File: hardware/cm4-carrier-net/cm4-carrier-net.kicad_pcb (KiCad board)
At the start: 4 copper layers, 90 x 40 mm, 42 parts, among them J1 USB_C_Receptacle_USB2.0, J2 Micro_SD_Card, J3 Abracon_ARJM11-502, Q1 DMP2066LSN, SW1 BOOT, SW2 GLOBAL_EN, U5 Compute_Module_4_Functional, U6 TPD2EUSB30

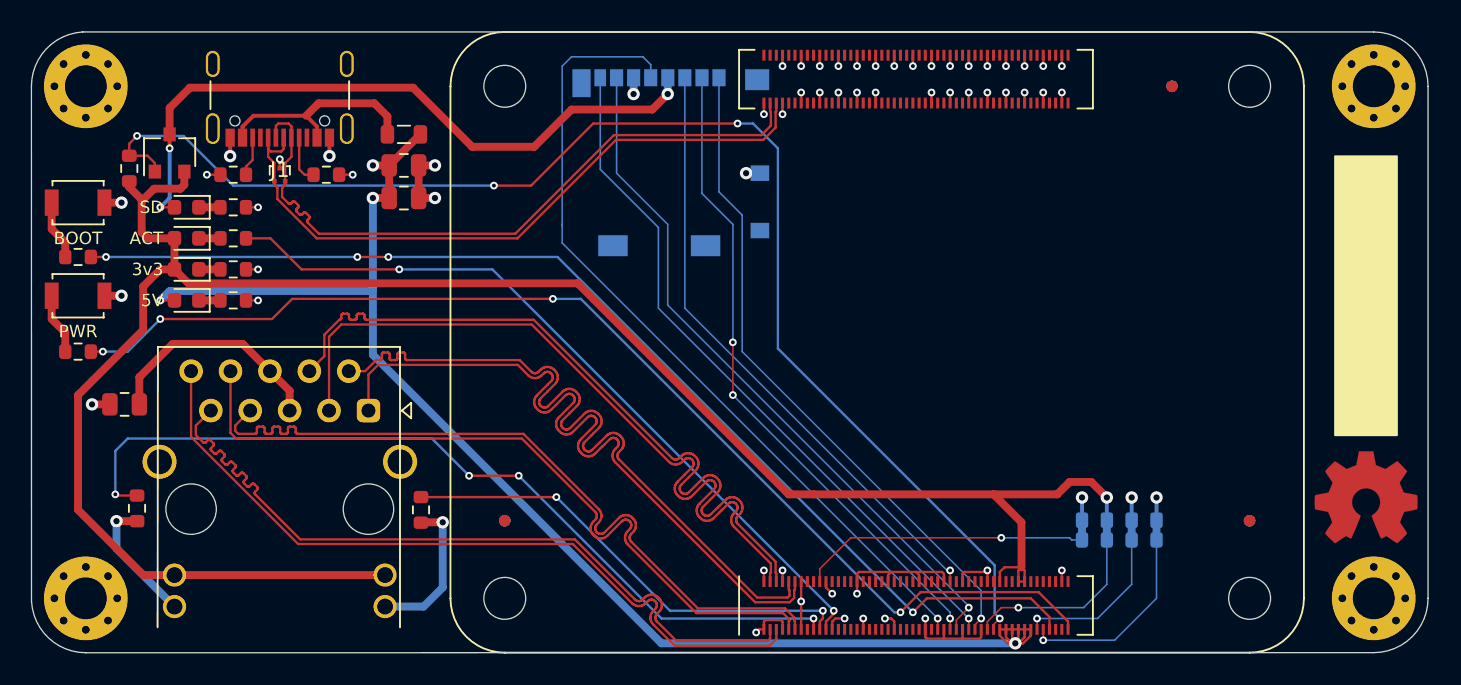
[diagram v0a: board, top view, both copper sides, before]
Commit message: Added USB OTG ID selection switch. Likely finalized v1.0a.
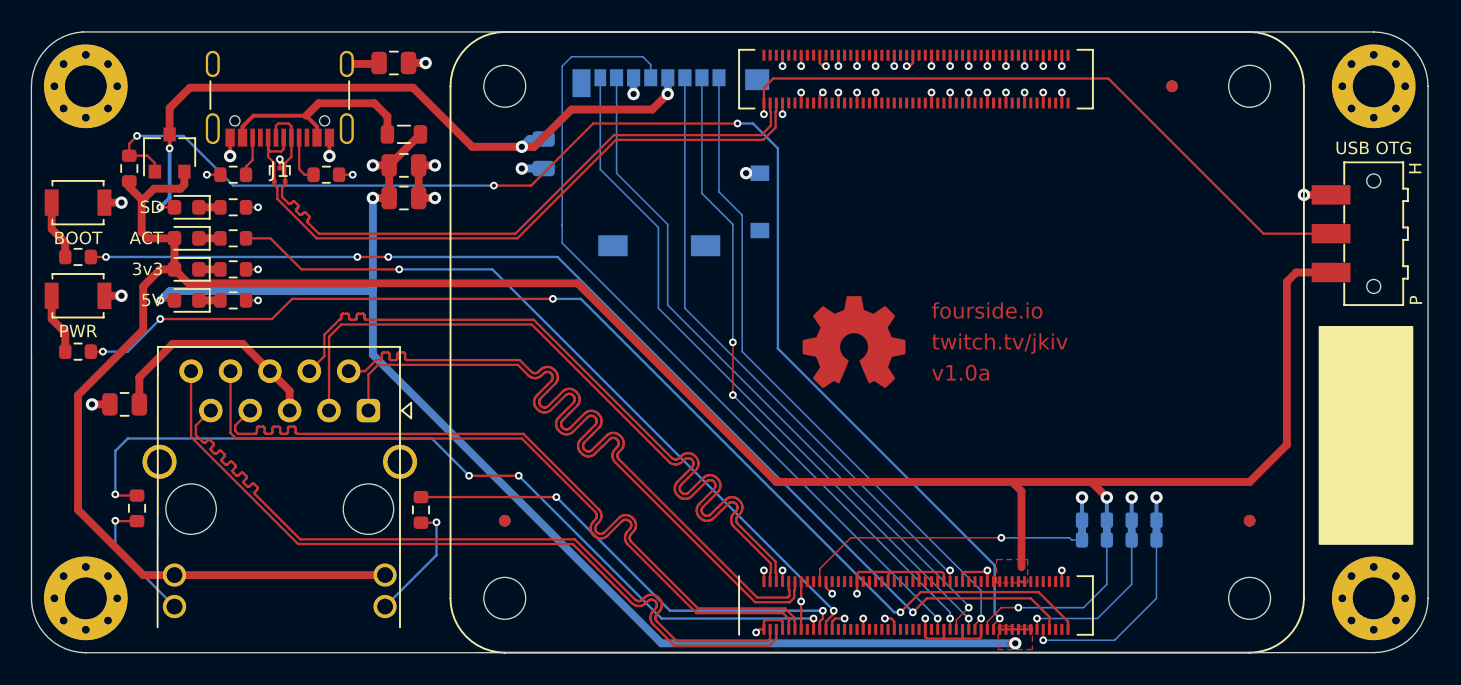
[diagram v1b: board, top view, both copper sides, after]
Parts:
- added C4: 22u, Capacitor_SMD:C_0805_2012Metric, B.Cu at (113.0, 101.8)
- added C5: 100n, Capacitor_SMD:C_0805_2012Metric, F.Cu at (103.3, 96.0)
- added SW3: USB_OTG, Button_Switch_SMD:SW_SPDT_CK-JS102011SAQN, F.Cu at (166.5, 107.0)
- moved LOGO1 34.5 mm to (133.0, 114.0)
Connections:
- U5 pad 101: GND -> /USB_OTG_ID
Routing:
- net /USB_OTG_ID: track 0.00 -> 42.6 mm, vias 0 -> 1
- net +3V3: track 130.4 -> 153.1 mm
- net +5V: track 90.9 -> 83.6 mm
- net GND: track 73.3 -> 77.5 mm, vias 61 -> 63
- net Net-(C5-Pad1): track 0.00 -> 2.10 mm
- net Net-(J3-Pad14): track 9.83 -> 7.81 mm
- net /SD_PWR: track 44.2 -> 45.8 mm, vias 3 -> 4
- added copper zone on F.Cu, net +3V3
- added copper zone on F.Cu, net +5V
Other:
- board text added: "H"
- board text added: "P"
- board text added: "USB OTG"
- board text added: "fourside.io"
- board text added: "twitch.tv/jkiv"
- board text added: "v1.0a"
